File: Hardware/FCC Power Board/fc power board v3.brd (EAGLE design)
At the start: 110 x 100 mm, 40 parts

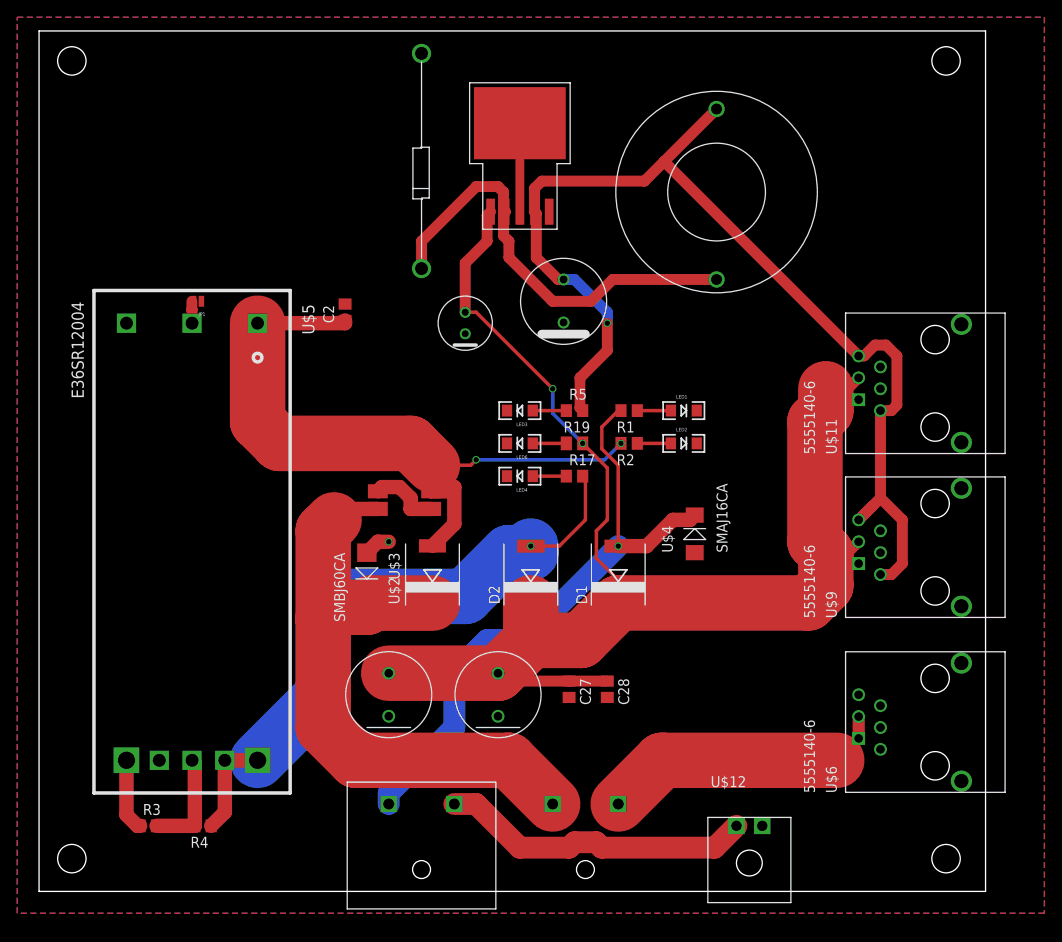
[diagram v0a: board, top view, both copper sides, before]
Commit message: cleaned up fc power board silk screen
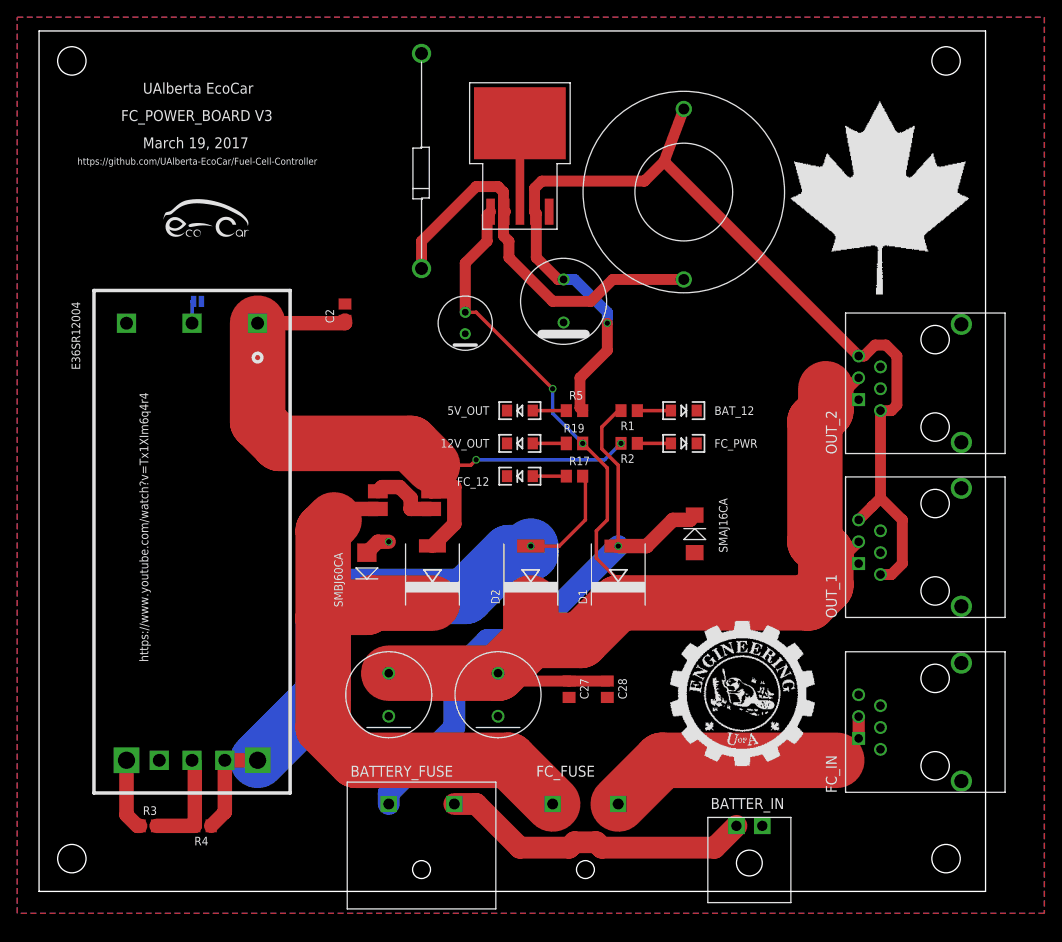
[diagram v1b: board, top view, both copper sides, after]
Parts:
- BATTER_IN: value 43650-0200 -> (none)
- FC_IN, OUT_1, OUT_2: value 5555140-6 -> (none)
- moved U$16 3.81 mm to (74.9, 71.1)
- flipped JP1 to the bottom, turned to 0 degrees
- renumbered LED1 to BAT_12, LED2 to FC_PWR, LED3 to 5V_OUT, LED4 to FC_12, LED6 to 12V_OUT, U$10 to BATTERY_FUSE, U$11 to OUT_2, U$12 to BATTER_IN, U$6 to FC_IN, U$9 to OUT_1
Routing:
- net 5V_OUT: track 130.0 -> 125.6 mm
- net N$7: track 50.9 -> 47.1 mm
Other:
- board text added: "BATTERY_FUSE"
- board text added: "FC_FUSE"
- board text added: "FC_POWER_BOARD V3"
- board text added: "March 19, 2017"
- board text added: "UAlberta EcoCar"
- board text added: "https://github.com/UAlberta-EcoCar/Fuel-Cell-Controller"
- board text added: "https://www.youtube.com/watch?v=Tx1XIm6q4r4"

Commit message: FC power board updated
updated board gerbers generated
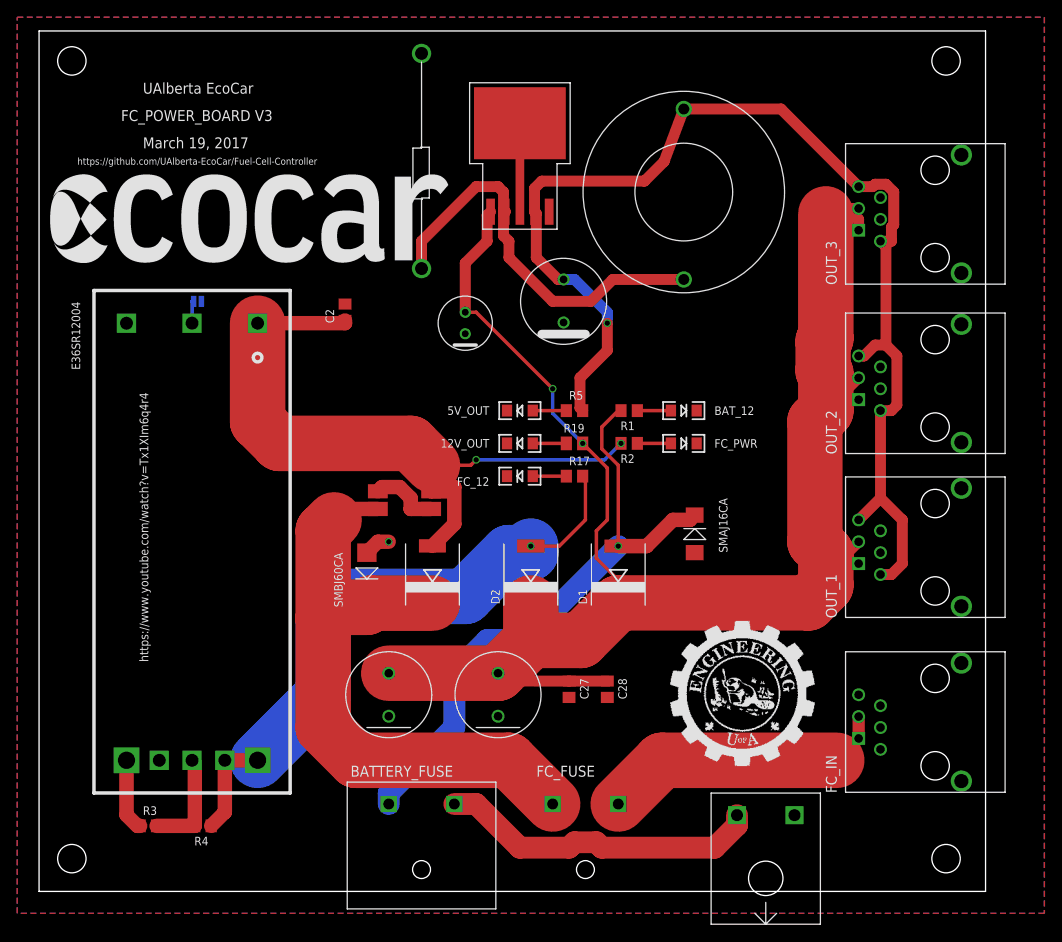
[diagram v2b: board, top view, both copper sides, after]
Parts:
- removed BATTER_IN: (no value), Shell2013:43650-0200
- added OUT_3: (no value), 5555140-6 RJ11:1734723-1_RJ11
- added U$6: (no value), ECOCAR_LOGO:ECOCAR_LOGO_2018
- added U$9: 2_PIN_TECONNECTOR, TE 2-pin connector:2_PIN_CONNECT
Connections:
- net 12V_OUT: now also OUT_3.1, OUT_3.2
- net 5V_OUT: now also OUT_3.3, OUT_3.4
- net BATT_IN: now also U$9.V/SIG; no longer BATTER_IN.P$1
- net GND: now also OUT_3.5, OUT_3.6, OUT_3.SH1, OUT_3.SH2, U$9.G/LOW; no longer BATTER_IN.P$2
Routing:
- net 12V_OUT: track 172.4 -> 200.1 mm
- net 5V_OUT: track 125.6 -> 141.7 mm
- net BATT_IN: track 36.5 -> 37.7 mm
